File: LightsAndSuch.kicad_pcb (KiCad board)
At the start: 4 copper layers, 80.3 x 76.8 mm, 84 parts, among them J1 Conn_01x02_Pin, J2 VIN, J3 TSA, J4 BMS Fault, J5 Button, J6 IMD Fault, J7 Break, P1 USB_C_Plug_USB2.0, Q1 AO3400A, Q2 AO3400A, Q3 AO3400A, Q4 AO3400A, Q5 AO3400A, U1 RP2040, U2 MAX98357A, U3 TPS54202DDC, U4 LM3940IMP-3.3, U5 CD4081BM, U6 LM555xM, U7 LM555xM, U8 W25Q128JVS, U9 NCP1117-3.3_SOT223

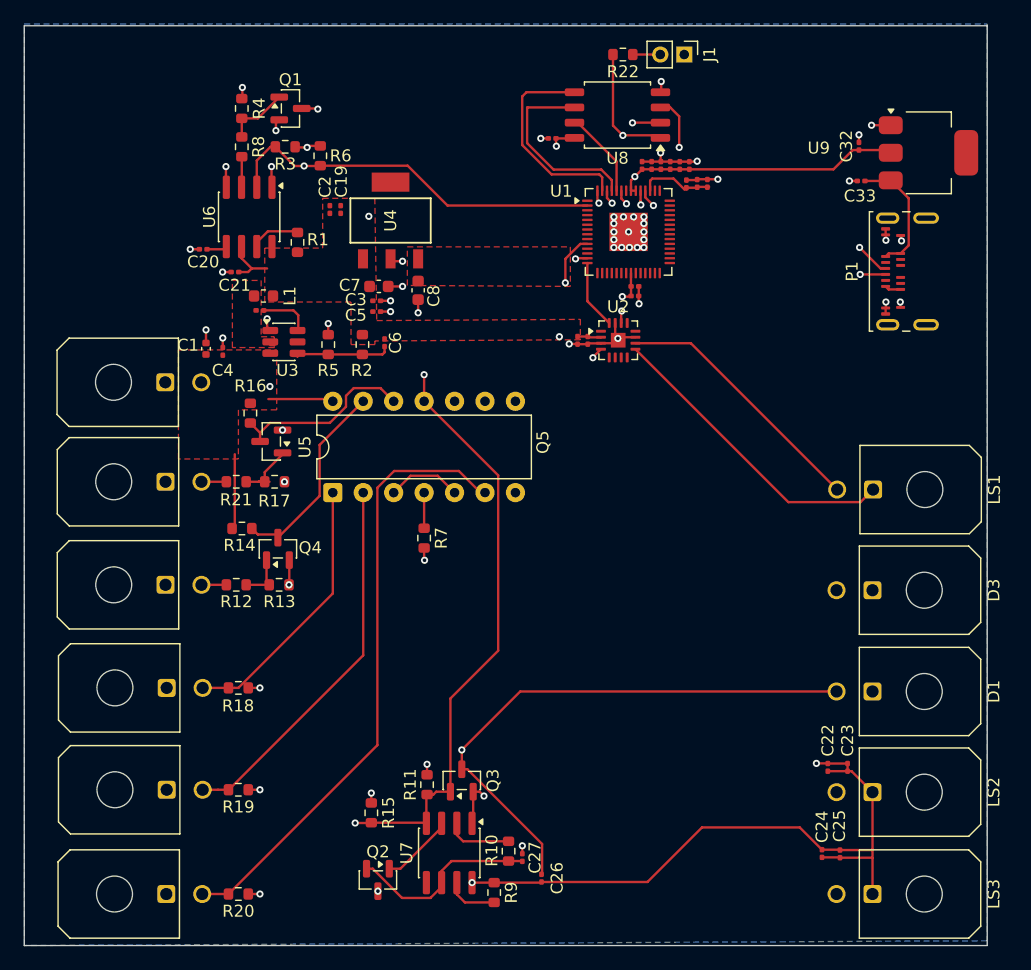
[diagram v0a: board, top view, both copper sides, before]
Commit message: slightly smaller board and thicker power lines
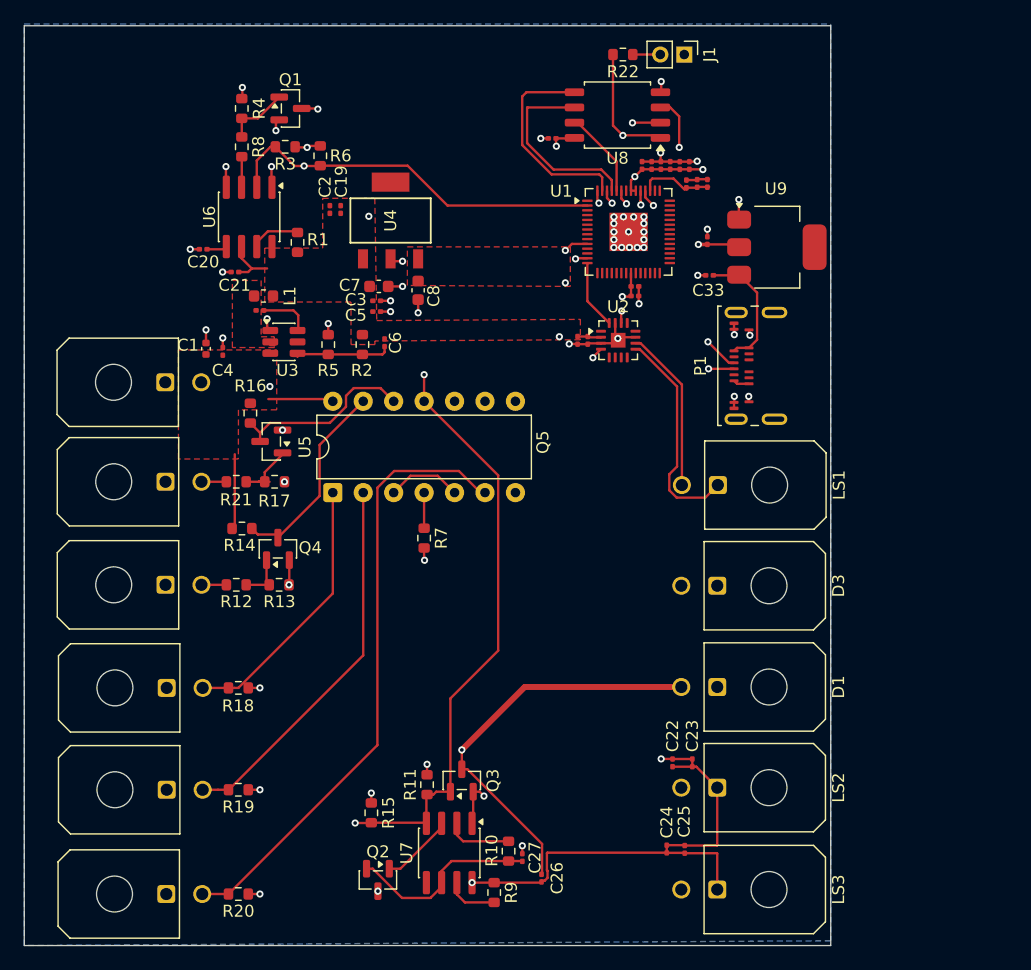
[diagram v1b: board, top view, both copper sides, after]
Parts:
- moved C32 14.9 mm to (114.5, 88.2)
- moved C33 14.9 mm to (114.7, 91.1)
- moved P1 14.9 mm to (119.9, 98.6)
- moved U9 14.9 mm to (120.3, 88.7)
- moved LS1 13.0 mm to (115.4, 108.6)
- moved C22 13.0 mm to (111.6, 131.8)
- moved C23 13.0 mm to (113.2, 131.8)
- moved C24 13.0 mm to (111.1, 138.9)
- moved C25 13.0 mm to (112.6, 139.0)
- moved D1 13.0 mm to (115.3, 125.4)
- moved D3 13.0 mm to (115.3, 117.0)
- moved LS2 13.0 mm to (115.3, 133.8)
- moved LS3 13.0 mm to (115.3, 142.3)
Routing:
- net +5V: track 107.9 -> 88.8 mm
- net +12V: track 124.0 -> 111.2 mm
- net Net-(D1-K): track 54.1 -> 45.1 mm
- net +3.3V: track 72.3 -> 63.6 mm, vias 5 -> 8
- net Net-(U2-OUTN): track 21.9 -> 13.7 mm
- net Net-(U2-OUTP): track 25.6 -> 18.4 mm
- net Net-(Q1-D): track 85.2 -> 79.7 mm
- net /USB_D-: track 24.1 -> 19.2 mm
- net /USB_D+: track 24.6 -> 21.1 mm
- net GND: track 53.1 -> 52.5 mm, vias 57 -> 56
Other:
- board size 80.3 x 76.8 mm -> 67.3 x 76.8 mm

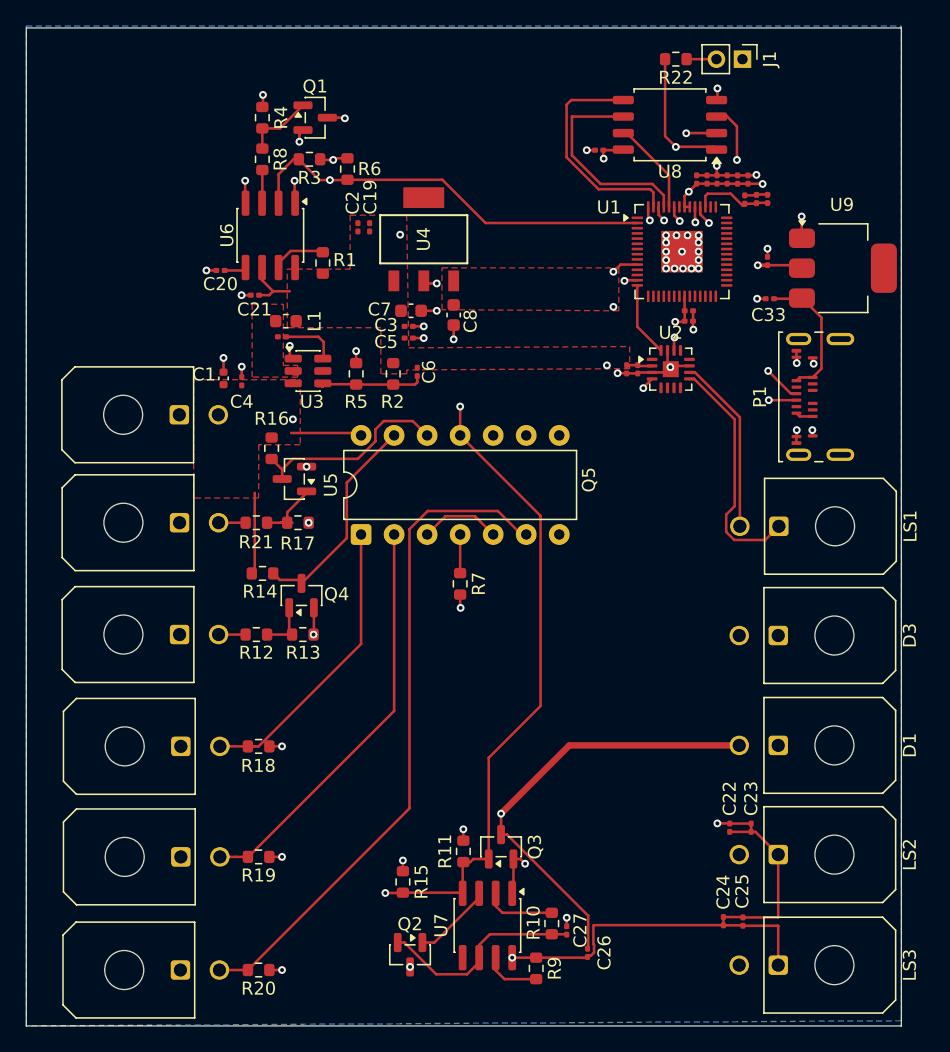
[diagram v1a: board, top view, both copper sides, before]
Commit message: switching out the connectors need to fix net names
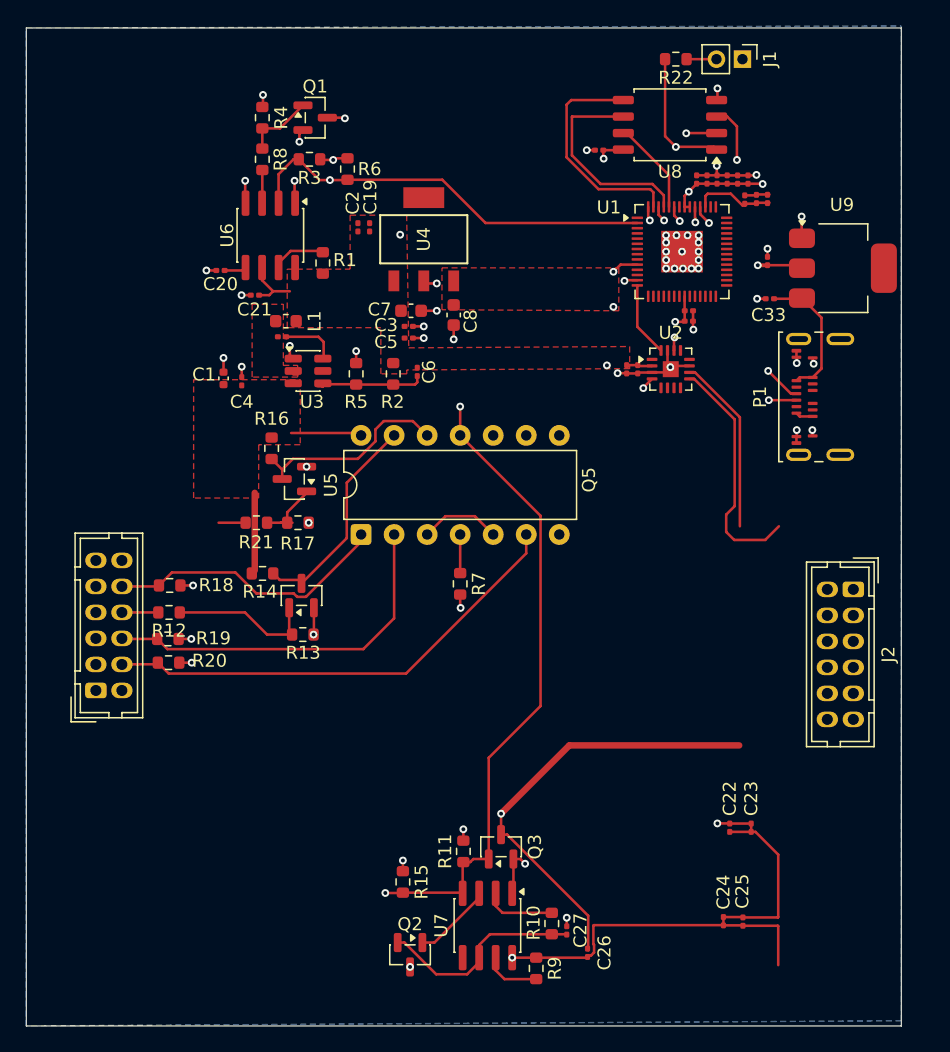
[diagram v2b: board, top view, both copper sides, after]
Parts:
- removed D1, D3: LED, Connector_Molex:Molex_Micro-Fit_3.0_43045-0200_2x01_P3.00mm_Horizontal
- removed J3: TSA, Connector_Molex:Molex_Micro-Fit_3.0_43045-0200_2x01_P3.00mm_Horizontal
- removed J4: BMS Fault, Connector_Molex:Molex_Micro-Fit_3.0_43045-0200_2x01_P3.00mm_Horizontal
- removed J5: Button, Connector_Molex:Molex_Micro-Fit_3.0_43045-0200_2x01_P3.00mm_Horizontal
- removed J6: IMD Fault, Connector_Molex:Molex_Micro-Fit_3.0_43045-0200_2x01_P3.00mm_Horizontal
- removed J7: Break, Connector_Molex:Molex_Micro-Fit_3.0_43045-0200_2x01_P3.00mm_Horizontal
- removed LS1: Speaker, Connector_Molex:Molex_Micro-Fit_3.0_43045-0200_2x01_P3.00mm_Horizontal
- removed LS2, LS3: MSO206NR, Connector_Molex:Molex_Micro-Fit_3.0_43045-0200_2x01_P3.00mm_Horizontal
- added J8: Conn_02x06_Odd_Even, Connector_Hirose:Hirose_DF11-12DP-2DSA_2x06_P2.00mm_Vertical, F.Cu at (62.9, 121.2)
- J2: value VIN -> Conn_02x06_Odd_Even; footprint Connector_Molex:Molex_Micro-Fit_3.0_43045-0200_2x01_P3.00mm_Horizontal -> Connector_Hirose:Hirose_DF11-12DP-2DSA_2x06_P2.00mm_Vertical
- moved J2 53.5 mm to (121.1, 113.4), turned to -90 degrees
- moved R20 24.6 mm to (68.4, 119.1)
- moved R19 18.2 mm to (68.4, 117.2)
- moved R18 14.1 mm to (68.5, 113.1)
- moved R12 6.93 mm to (68.5, 115.2)
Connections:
- C1 pad 1: +12V -> FAULT_ANODE
- C1 pad 2: GND -> OK_CATHODE
- C10 pad 2: GND -> OK_CATHODE
- C11 pad 2: GND -> OK_CATHODE
- C12 pad 2: GND -> OK_CATHODE
- C13 pad 2: GND -> OK_CATHODE
- C14 pad 2: GND -> OK_CATHODE
- C15 pad 2: GND -> OK_CATHODE
- C16 pad 2: GND -> OK_CATHODE
- C17 pad 1: GND -> OK_CATHODE
- C17 pad 2: +5V -> LS2_P
- C18 pad 1: GND -> OK_CATHODE
- C18 pad 2: +5V -> LS2_P
- C19 pad 1: +5V -> LS2_P
- C19 pad 2: +5V -> LS2_P
- C2 pad 1: +5V -> LS2_P
- C2 pad 2: +5V -> LS2_P
- C20 pad 2: GND -> OK_CATHODE
- C21 pad 1: GND -> OK_CATHODE
- C21 pad 2: +5V -> LS2_P
- C22 pad 1: +5V -> LS2_P
- C22 pad 2: +5V -> LS2_P
- C23 pad 1: +5V -> LS2_P
- C23 pad 2: +5V -> LS2_P
- C24 pad 1: +5V -> LS2_P
- C24 pad 2: +5V -> LS2_P
- C25 pad 1: +5V -> LS2_P
- C25 pad 2: +5V -> LS2_P
- C26 pad 1: +5V -> LS2_P
- C26 pad 2: +12V -> FAULT_ANODE
- C27 pad 1: GND -> OK_CATHODE
- C28 pad 2: GND -> OK_CATHODE
- C29 pad 2: GND -> OK_CATHODE
- C3 pad 1: +5V -> LS2_P
- C3 pad 2: GND -> OK_CATHODE
- C30 pad 2: GND -> OK_CATHODE
- C31 pad 2: GND -> OK_CATHODE
- C32 pad 2: GND -> OK_CATHODE
- C33 pad 2: GND -> OK_CATHODE
- C4 pad 1: +12V -> FAULT_ANODE
- C4 pad 2: GND -> OK_CATHODE
- C5 pad 1: +5V -> LS2_P
- C5 pad 2: GND -> OK_CATHODE
- C6 pad 1: +5V -> LS2_P
- C7 pad 1: +5V -> LS2_P
- C7 pad 2: GND -> OK_CATHODE
- C8 pad 2: GND -> OK_CATHODE
- C9 pad 1: GND -> OK_CATHODE
- J1 pad 1: GND -> OK_CATHODE
- J2 pad 1: GND -> LS1_P
- J2 pad 2: +12V -> LS1_N
- L1 pad 2: +5V -> LS2_P
- P1 pad A1: GND -> OK_CATHODE
- P1 pad A12: GND -> OK_CATHODE
- P1 pad B1: GND -> OK_CATHODE
- P1 pad B12: GND -> OK_CATHODE
- P1 pad S1: GND -> OK_CATHODE
- Q1 pad 2: GND -> OK_CATHODE
- Q1 pad 3: Net-(Q1-D) -> LS2_n
- Q2 pad 3: Net-(D1-K) -> FAULT_CATHODE
- Q3 pad 2: GND -> OK_CATHODE
- Q3 pad 3: +12V -> FAULT_ANODE
- Q4 pad 2: GND -> OK_CATHODE
- Q5 pad 2: GND -> OK_CATHODE
- R1 pad 1: +5V -> LS2_P
- R11 pad 1: GND -> OK_CATHODE
- R13 pad 2: GND -> OK_CATHODE
- R14 pad 1: +12V -> FAULT_ANODE
- R15 pad 1: GND -> OK_CATHODE
- R16 pad 1: +12V -> FAULT_ANODE
- R17 pad 2: GND -> OK_CATHODE
- R18 pad 1: GND -> OK_CATHODE
- R19 pad 1: GND -> OK_CATHODE
- R2 pad 1: +5V -> LS2_P
- R20 pad 1: GND -> OK_CATHODE
- R3 pad 1: GND -> OK_CATHODE
- R4 pad 2: GND -> OK_CATHODE
- R5 pad 2: GND -> OK_CATHODE
- R6 pad 2: GND -> OK_CATHODE
- R9 pad 1: +5V -> LS2_P
- U1 pad 57: GND -> OK_CATHODE
- U2 pad 10: Net-(U2-OUTN) -> LS1_N
- U2 pad 11: GND -> OK_CATHODE
- U2 pad 15: GND -> OK_CATHODE
- U2 pad 17: GND -> OK_CATHODE
- U2 pad 2: +5V -> LS2_P
- U2 pad 3: GND -> OK_CATHODE
- U2 pad 7: (no net) -> LS2_P
- U2 pad 8: (no net) -> LS2_P
- U2 pad 9: Net-(U2-OUTP) -> LS1_P
- U3 pad 1: GND -> OK_CATHODE
- U3 pad 3: +12V -> FAULT_ANODE
- U4 pad 1: +5V -> LS2_P
- U4 pad 2: GND -> OK_CATHODE
- U5 pad 14: +12V -> FAULT_ANODE
- U5 pad 7: GND -> OK_CATHODE
- U6 pad 1: GND -> OK_CATHODE
- U6 pad 4: GND -> OK_CATHODE
- U6 pad 6: +5V -> LS2_P
- U6 pad 8: +5V -> LS2_P
- U7 pad 1: GND -> OK_CATHODE
- U7 pad 8: +5V -> LS2_P
- U8 pad 4: GND -> OK_CATHODE
- U9 pad 1: GND -> OK_CATHODE
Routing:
- net +12V: track 111.2 -> 0.00 mm, vias 2 -> 0
- net LS2_P: track 0.00 -> 88.8 mm, vias 0 -> 4
- net +5V: track 88.8 -> 0.00 mm, vias 4 -> 0
- net Net-(Q1-D): track 79.7 -> 0.00 mm, vias 1 -> 0
- net FAULT_ANODE: track 0.00 -> 79.5 mm, vias 0 -> 1
- net LS2_n: track 0.00 -> 70.9 mm, vias 0 -> 1
- net GND: track 52.5 -> 0.00 mm, vias 56 -> 0
- net OK_CATHODE: track 0.00 -> 52.5 mm, vias 0 -> 56
- net Net-(D1-K): track 45.1 -> 0.00 mm, vias 1 -> 0
- net FAULT_CATHODE: track 0.00 -> 45.1 mm, vias 0 -> 1
- net Net-(U2-OUTP): track 18.4 -> 0.00 mm
- net LS1_P: track 0.00 -> 18.4 mm
- net (no net): track 0.00 -> 17.2 mm
- net Button: track 51.5 -> 37.1 mm
- net Net-(U2-OUTN): track 13.7 -> 0.00 mm
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- added copper zone on F.Cu, net FAULT_ANODE
- added copper zone on F.Cu, net LS2_P
- added copper zone on B.Cu, net OK_CATHODE
- added copper zone on In1.Cu, net OK_CATHODE
- added copper zone on In2.Cu, net OK_CATHODE
- removed copper zone on F.Cu, net +12V
- removed copper zone on F.Cu, net +5V
- removed copper zone on B.Cu, net GND
- removed copper zone on In1.Cu, net GND
- removed copper zone on In2.Cu, net GND
